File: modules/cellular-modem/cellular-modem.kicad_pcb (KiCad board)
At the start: 2 copper layers, 4 parts, among them J1 Bus_PCI_Express_Mini, U1 TXV0108RGYR, U2 TXV0108RGYR, U3 TXV0108RGYR

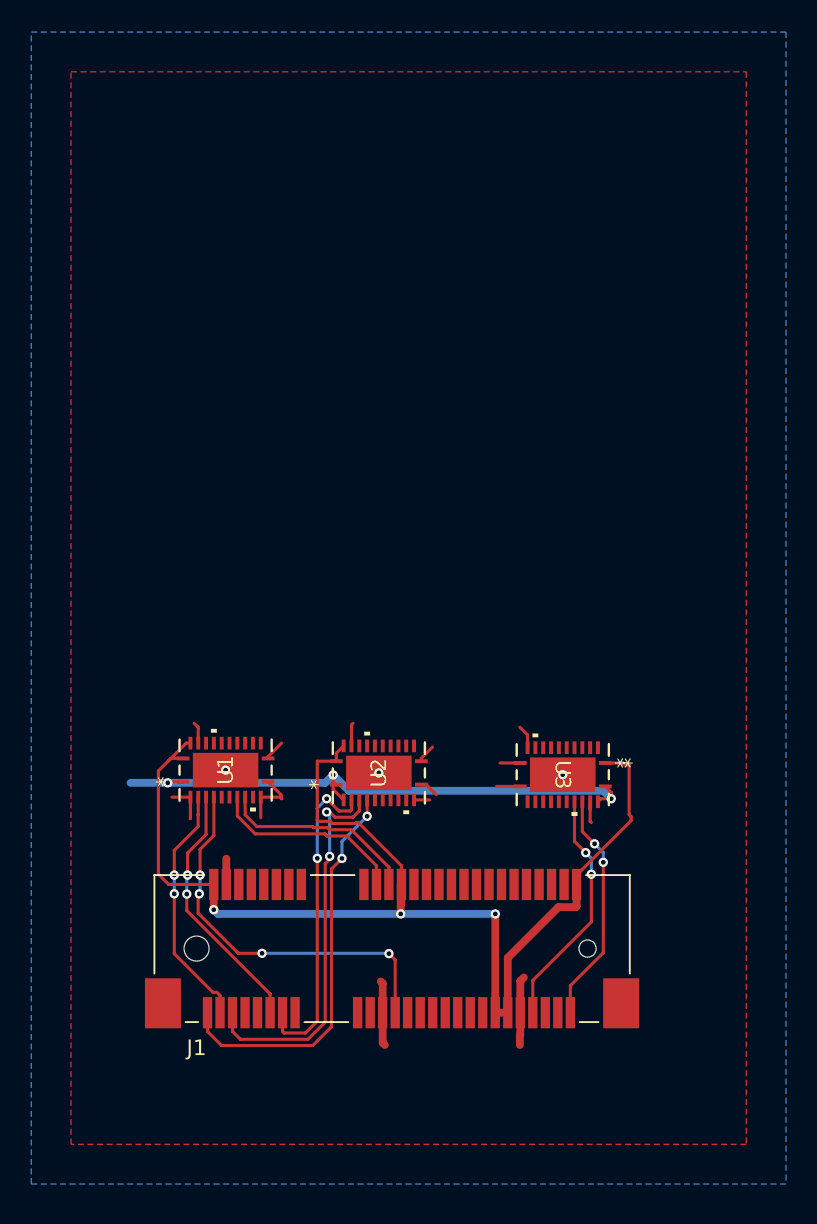
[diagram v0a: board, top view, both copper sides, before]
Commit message: layout USB lines to alegedly have correct impedance
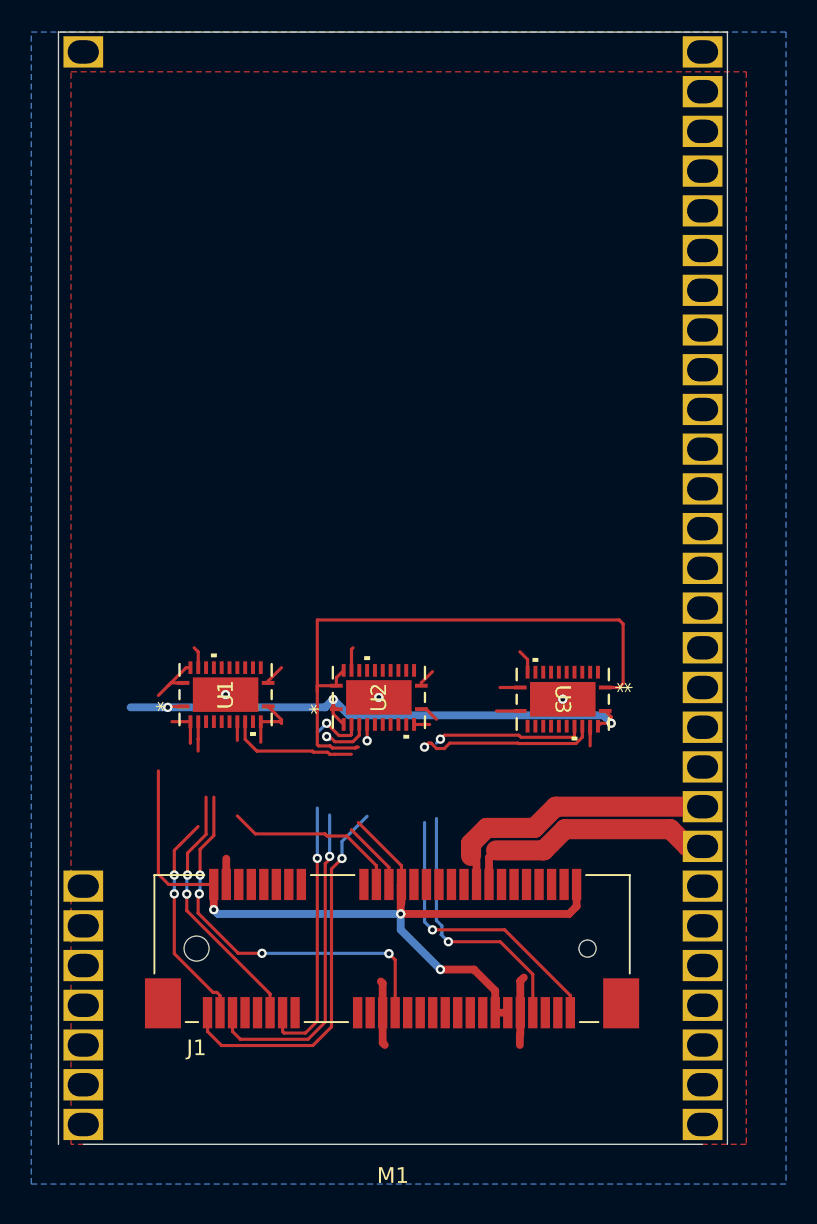
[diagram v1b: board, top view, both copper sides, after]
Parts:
- added M1: ~, MegaCastle:MegaCastle2x28-Module-I36.0x66.3-M800007FFFFFFFF-NIBBLE, F.Cu at (89.2, 71.1)
- moved U1 4.83 mm to (78.5, 77.9)
- moved U3 4.83 mm to (100.0, 78.2)
- moved U2 4.83 mm to (88.3, 78.1)
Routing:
- net 3V3: track 79.5 -> 98.0 mm
- net USB_D-: track 0.00 -> 18.1 mm
- net USB_D+: track 0.00 -> 16.6 mm
- net /PCM_SYNC_1V8_IO: track 14.9 -> 30.1 mm
- net /PCM_CLK_1V8_IO: track 15.5 -> 26.7 mm
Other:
- board outline added: 42.8 x 71.1 mm

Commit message: add 3.3V and 1.8V DC:DC to cellular modem module
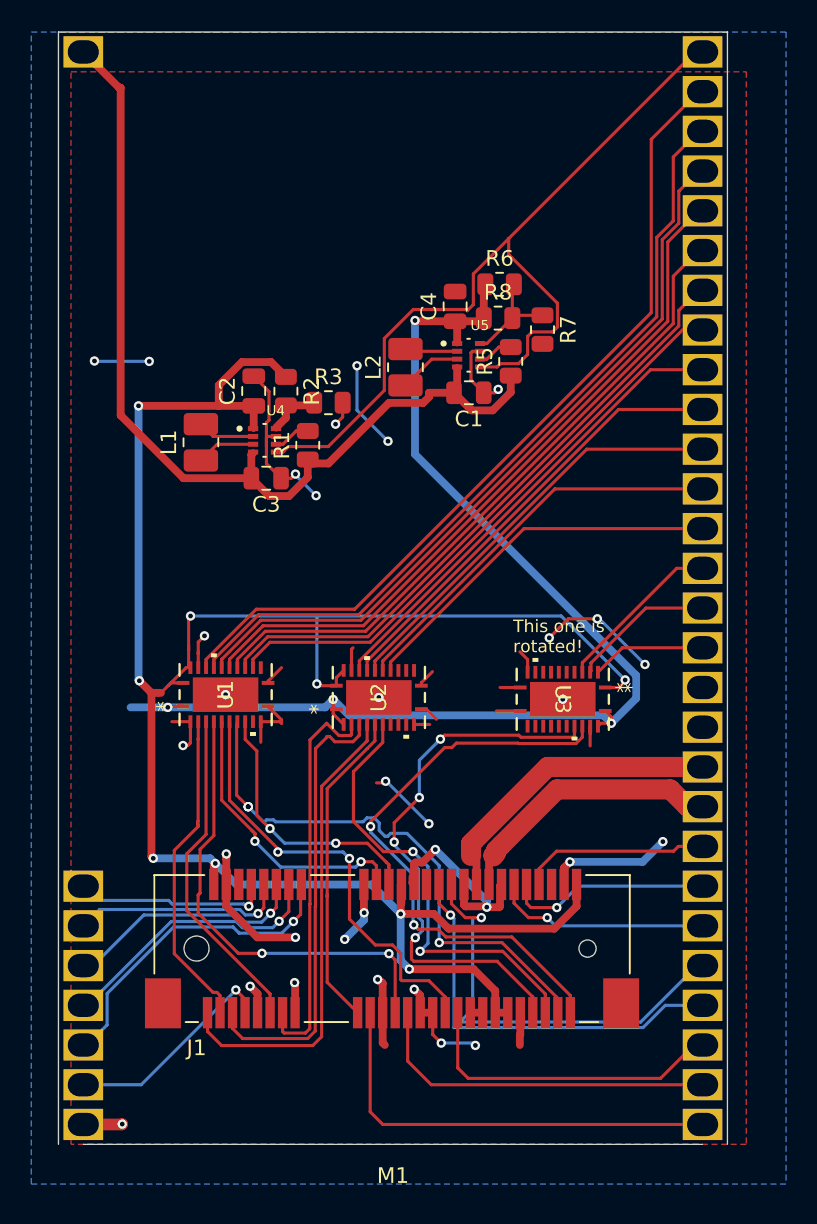
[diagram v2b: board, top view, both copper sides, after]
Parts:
- added C1: 47uF, Capacitor_SMD:C_0805_2012Metric, F.Cu at (94.0, 58.6)
- added C2: 15uF, Capacitor_SMD:C_0805_2012Metric, F.Cu at (80.3, 58.5)
- added C3: 47uF, Capacitor_SMD:C_0805_2012Metric, F.Cu at (81.1, 64.1)
- added C4: 15uF, Capacitor_SMD:C_0805_2012Metric, F.Cu at (93.1, 53.1)
- added L1: 1uH, Inductor_SMD:L_1008_2520Metric_Pad1.43x2.20mm_HandSolder, F.Cu at (76.9, 61.8)
- added L2: 1uH, Inductor_SMD:L_1008_2520Metric_Pad1.43x2.20mm_HandSolder, F.Cu at (90.0, 57.0)
- added R1: 510K, Resistor_SMD:R_0805_2012Metric, F.Cu at (83.7, 62.0)
- added R2: 510K, Resistor_SMD:R_0805_2012Metric, F.Cu at (82.3, 58.5)
- added R3: 90.9K, Resistor_SMD:R_0805_2012Metric, F.Cu at (85.0, 59.3)
- added R5: 510K, Resistor_SMD:R_0805_2012Metric, F.Cu at (96.7, 56.6)
- added R6: 510K, Resistor_SMD:R_0805_2012Metric, F.Cu at (96.0, 51.7)
- added R7: 90.9K, Resistor_SMD:R_0805_2012Metric, F.Cu at (98.7, 54.6)
- added R8: 432K, Resistor_SMD:R_0805_2012Metric, F.Cu at (95.9, 53.8)
- added U4: TPS631000DRLR, cellular-modem:SOT50P160X60-8N, F.Cu at (81.0, 61.7)
- added U5: TPS631000DRLR, cellular-modem:SOT50P160X60-8N, F.Cu at (94.0, 56.2)
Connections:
- J1 pad 25: unconnected-(J1-PERp0-Pad25) -> PERp0
- M1 pad 22: unconnected-(M1-Pad22) -> USIM_VDD
- M1 pad 23: unconnected-(M1-Pad23) -> USIM_DATA
- M1 pad 24: unconnected-(M1-Pad24) -> USIM_CLK
- M1 pad 25: unconnected-(M1-Pad25) -> /USIM_RESET
- M1 pad 26: unconnected-(M1-Pad26) -> USIM_VPP
- M1 pad 27: unconnected-(M1-Pad27) -> /CLKREQ
- M1 pad 29: unconnected-(M1-Pad29) -> EN
- M1 pad 30: unconnected-(M1-Pad30) -> COEX_UART_RX_3V3
- M1 pad 31: unconnected-(M1-Pad31) -> UART_RX_3V3
- M1 pad 32: unconnected-(M1-Pad32) -> UART_CTS_3V3
- M1 pad 33: unconnected-(M1-Pad33) -> /W_DISABLE_3V3
- M1 pad 34: unconnected-(M1-Pad34) -> /DTR_SLEEP_MODE_3V3
- M1 pad 35: unconnected-(M1-Pad35) -> PCM_DIN_3V3
- M1 pad 36: unconnected-(M1-Pad36) -> /RESET_3V3
- M1 pad 37: unconnected-(M1-Pad37) -> UART_TX_3V3
- M1 pad 38: unconnected-(M1-Pad38) -> COEX_UART_TX_3V3
- M1 pad 39: unconnected-(M1-Pad39) -> /WAKE_3V3
- M1 pad 40: unconnected-(M1-Pad40) -> RI_HOST_WAKE_3V3
- M1 pad 41: unconnected-(M1-Pad41) -> PCM_DOUT_3V3
- M1 pad 42: unconnected-(M1-Pad42) -> PCM_CLK_3V3
- M1 pad 43: unconnected-(M1-Pad43) -> PCM_SYNC_3V#
- M1 pad 44: unconnected-(M1-Pad44) -> PCM_CLK_DIR
- M1 pad 47: unconnected-(M1-Pad47) -> USB_D-
- M1 pad 48: USB_D- -> USB_D+
- M1 pad 49: USB_D+ -> RESERVED_PIN46
- M1 pad 50: unconnected-(M1-Pad50) -> USIM_SIM_PRESENT_IN
- M1 pad 51: unconnected-(M1-Pad51) -> /LED_WWAN_OC_OUT
- M1 pad 52: unconnected-(M1-Pad52) -> I2C_DATA_1V8
- M1 pad 53: unconnected-(M1-Pad53) -> I2C_SCL_1V8
- M1 pad 54: unconnected-(M1-Pad54) -> PETp0
- M1 pad 55: unconnected-(M1-Pad55) -> PERp0
- M1 pad 56: unconnected-(M1-Pad56) -> RESERVED_PIN19
- U1 pad 16: /W_DISABLE_3V3 -> PCM_DIN_3V3
- U1 pad 17: PCM_DIN_3V3 -> /DTR_SLEEP_MODE_3V3
- U1 pad 18: /DTR_SLEEP_MODE_3V3 -> /W_DISABLE_3V3
- U1 pad 6: //DTR_SLEEP_MODE_1V8_IN -> //W_DISABLE_1V8_IN
- U1 pad 7: /PCM_DIN_1V8_IN -> //DTR_SLEEP_MODE_1V8_IN
- U1 pad 8: //W_DISABLE_1V8_IN -> /PCM_DIN_1V8_IN
- U2 pad 17: RI_HOST_WAKE_3V3 -> PCM_DOUT_3V3
- U2 pad 18: PCM_DOUT_3V3 -> RI_HOST_WAKE_3V3
- U2 pad 6: /PCM_DOUT_1V8_OUT -> /RI_HOST_WAKE_1V8_OUT
- U2 pad 7: /RI_HOST_WAKE_1V8_OUT -> /PCM_DOUT_1V8_OUT
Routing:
- net GND: track 30.6 -> 112.5 mm, vias 3 -> 31
- net VBAT: track 0.00 -> 60.6 mm
- net EN: track 0.00 -> 54.7 mm
- net COEX_UART_RX_3V3: track 0.00 -> 53.8 mm
- net UART_RX_3V3: track 0.00 -> 51.1 mm
- net UART_CTS_3V3: track 0.00 -> 48.4 mm
- net /W_DISABLE_3V3: track 0.00 -> 45.6 mm
- net /DTR_SLEEP_MODE_3V3: track 0.00 -> 42.9 mm
- net 3V3: track 98.0 -> 138.6 mm, vias 3 -> 9
- net 1V8: track 36.6 -> 77.2 mm, vias 3 -> 4
- net PCM_DIN_3V3: track 0.00 -> 40.1 mm
- net /RESET_3V3: track 0.00 -> 38.0 mm
- net /PCM_DIN_1V8_IN: track 0.00 -> 35.2 mm, vias 0 -> 3
- net UART_TX_3V3: track 0.00 -> 30.3 mm
- net /PCM_DOUT_1V8_OUT: track 0.00 -> 28.9 mm, vias 0 -> 2
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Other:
- board text added: "This one is rotated!"

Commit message: relocate footprints to root dir of module
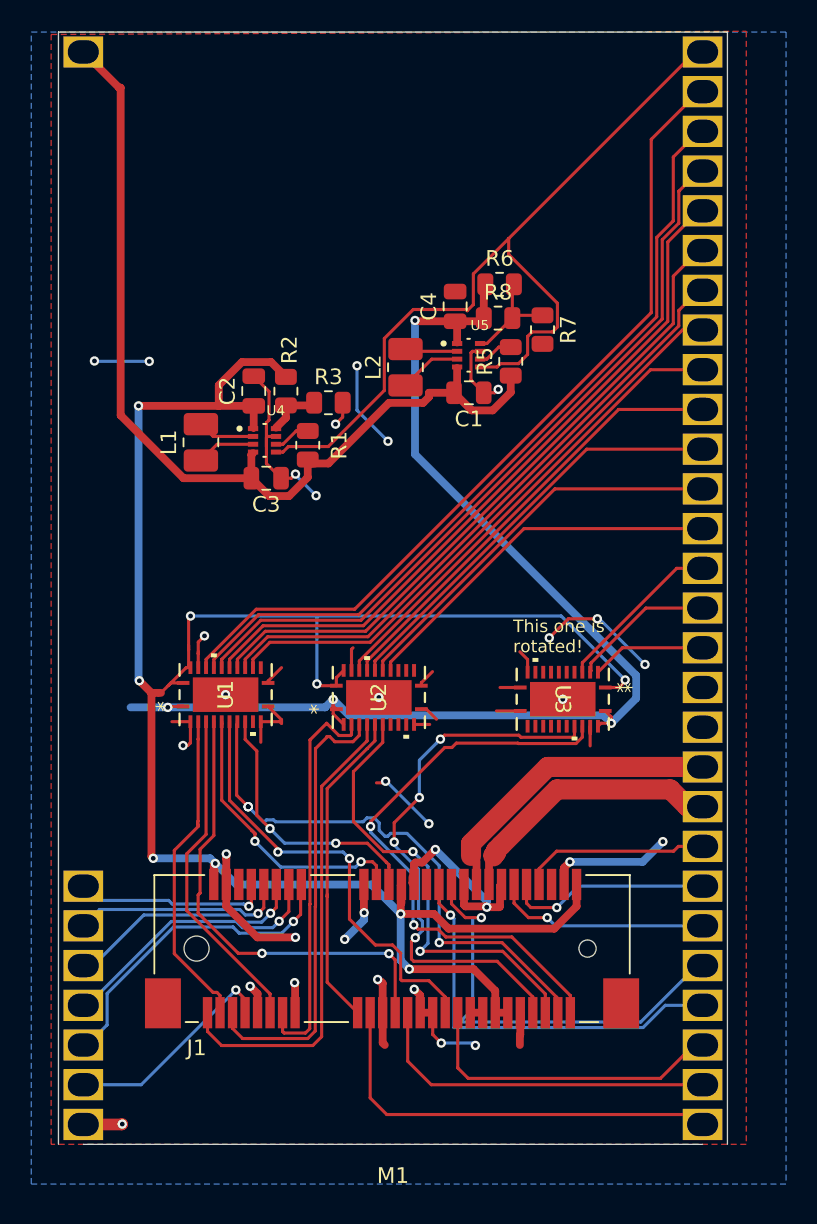
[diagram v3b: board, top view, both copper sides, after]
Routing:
- net RESERVED_PIN19: track 27.9 -> 27.4 mm
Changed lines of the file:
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@@
 		)
 		(property "Value" "TPS631000DRLR"
-			(at 4.781 1.8436 0)
-			(layer "F.Fab")
+			(at -2.2152 1.83316 90)
+			(layer "B.SilkS")
 			(effects
 				(font
@@
 					(thickness 0.15)
 				)
+				(justify mirror)
 			)
 		)
@@
 		)
 		(property "Value" "1uH"
-			(at 0 2.05 90)
-			(layer "F.Fab")
+			(at 0 0 90)
+			(layer "B.SilkS")
 			(effects
 				(font
@@
 					(thickness 0.15)
 				)
+				(justify mirror)
 			)
 		)
@@
 		)
 		(property "Value" "90.9K"
-			(at 0 1.65 90)
-			(layer "F.Fab")
+			(at 0 0 90)
+			(layer "B.SilkS")
 			(effects
 				(font
@@
 					(thickness 0.15)
 				)
+				(justify mirror)
 			)
 		)
@@
 		)
 		(property "Value" "47uF"
-			(at 0 1.68 360)
-			(layer "F.Fab")
+			(at 0.0406 -0.4318 0)
+			(layer "B.SilkS")
 			(effects
 				(font
@@
 					(thickness 0.15)
 				)
+				(justify mirror)
 			)
 		)
@@
 		)
 		(property "Value" "510K"
-			(at 0 1.65 90)
-			(layer "F.Fab")
+			(at 0 0.4572 90)
+			(layer "B.SilkS")
 			(effects
 				(font
@@
 					(thickness 0.15)
 				)
+				(justify mirror)
 			)
 		)
@@
 		)
 		(property "Value" "432K"
-			(at 0 1.65 0)
-			(layer "F.Fab")
+			(at 0 0 0)
+			(layer "B.SilkS")
 			(effects
 				(font
@@
 					(thickness 0.15)
 				)
+				(justify mirror)
 			)
 		)
@@
 		)
 		(property "Value" "1uH"
-			(at 0 2.05 90)
-			(layer "F.Fab")
+			(at 0 0 90)
+			(layer "B.SilkS")
 			(effects
 				(font
@@
 					(thickness 0.15)
 				)
+				(justify mirror)
 			)
 		)
@@
 		)
 		(property "Value" "510K"
-			(at 0 1.65 0)
-			(layer "F.Fab")
+			(at 0 0 0)
+			(layer "B.SilkS")
 			(effects
 				(font
@@
 					(thickness 0.15)
 				)
+				(justify mirror)
 			)
 		)
@@
 		)
 		(property "Value" "90.9K"
-			(at 0 1.65 360)
-			(layer "F.Fab")
+			(at 0.6858 -0.20464 0)
+			(layer "B.SilkS")
 			(effects
 				(font
@@
 					(thickness 0.15)
 				)
+				(justify mirror)
 			)
 		)
@@
 		(tags "resistor")
 		(property "Reference" "R1"
-			(at 0 -1.65 90)
+			(at 0 2.0066 90)
 			(layer "F.SilkS")
 			(effects
@@
 		)
 		(property "Value" "510K"
-			(at 0 1.65 90)
-			(layer "F.Fab")
+			(at 0 0.1016 90)
+			(layer "B.SilkS")
 			(effects
 				(font
@@
 					(thickness 0.15)
 				)
+				(justify mirror)
 			)
 		)
@@
 		(tags "resistor")
 		(property "Reference" "R2"
-			(at 0 -1.65 90)
+			(at -2.64114 -0.2286 90)
 			(layer "F.SilkS")
 			(effects
@@
 		)
 		(property "Value" "510K"
-			(at 0 1.65 90)
-			(layer "F.Fab")
+			(at -0.10114 -0.2286 90)
+			(layer "B.SilkS")
 			(effects
 				(font
@@
 					(thickness 0.15)
 				)
+				(justify mirror)
 			)
 		)
@@
 		)
 		(property "Value" "TPS631000DRLR"
-			(at 4.781 1.8436 0)
-			(layer "F.Fab")
+			(at -2.5638 2.1964 90)
+			(layer "B.SilkS")
 			(effects
 				(font
@@
 					(thickness 0.15)
 				)
+				(justify mirror)
 			)
 		)
@@
 		)
 		(property "Value" "15uF"
-			(at 0 1.68 90)
-			(layer "F.Fab")
+			(at 0 0 90)
+			(layer "B.SilkS")
 			(effects
 				(font
@@
 					(thickness 0.15)
 				)
+				(justify mirror)
 			)
 		)
@@
 		)
 		(property "Value" "15uF"
-			(at 0 1.68 90)
-			(layer "F.Fab")
+			(at 0 0 90)
+			(layer "B.SilkS")
 			(effects
 				(font
@@
 					(thickness 0.15)
 				)
+				(justify mirror)
 			)
 		)
@@
 		)
 		(property "Value" "47uF"
-			(at 0 1.68 360)
-			(layer "F.Fab")
+			(at -0.2184 -0.68436 0)
+			(layer "B.SilkS")
 			(effects
 				(font
@@
 					(thickness 0.15)
 				)
+				(justify mirror)
 			)
 		)
@@
 	)
 	(segment
-		(start 88.519 105.41)
+		(start 87.709 98.263)
+		(end 87.709 103.711)
+		(width 0.2)
+		(layer "F.Cu")
+		(net 31)
+	)
+	(segment
+		(start 108.331 104.775)
 		(end 108.966 105.41)
 		(width 0.2)
@@
 	)
 	(segment
-		(start 87.709 98.263)
-		(end 87.709 104.6)
+		(start 88.773 104.775)
+		(end 108.331 104.775)
 		(width 0.2)
 		(layer "F.Cu")
@@
 	)
 	(segment
-		(start 87.709 104.6)
-		(end 88.519 105.41)
+		(start 87.709 103.711)
+		(end 88.773 104.775)
 		(width 0.2)
 		(layer "F.Cu")
@@
 		(polygon
 			(pts
-				(xy 68.58 38.1) (xy 111.76 38.1) (xy 111.76 106.68) (xy 68.58 106.68)
+				(xy 67.31 35.7124) (xy 111.76 35.5092) (xy 111.76 106.68) (xy 67.31 106.68)
 			)
 		)

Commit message: add footprints etc for miniPCIe connector
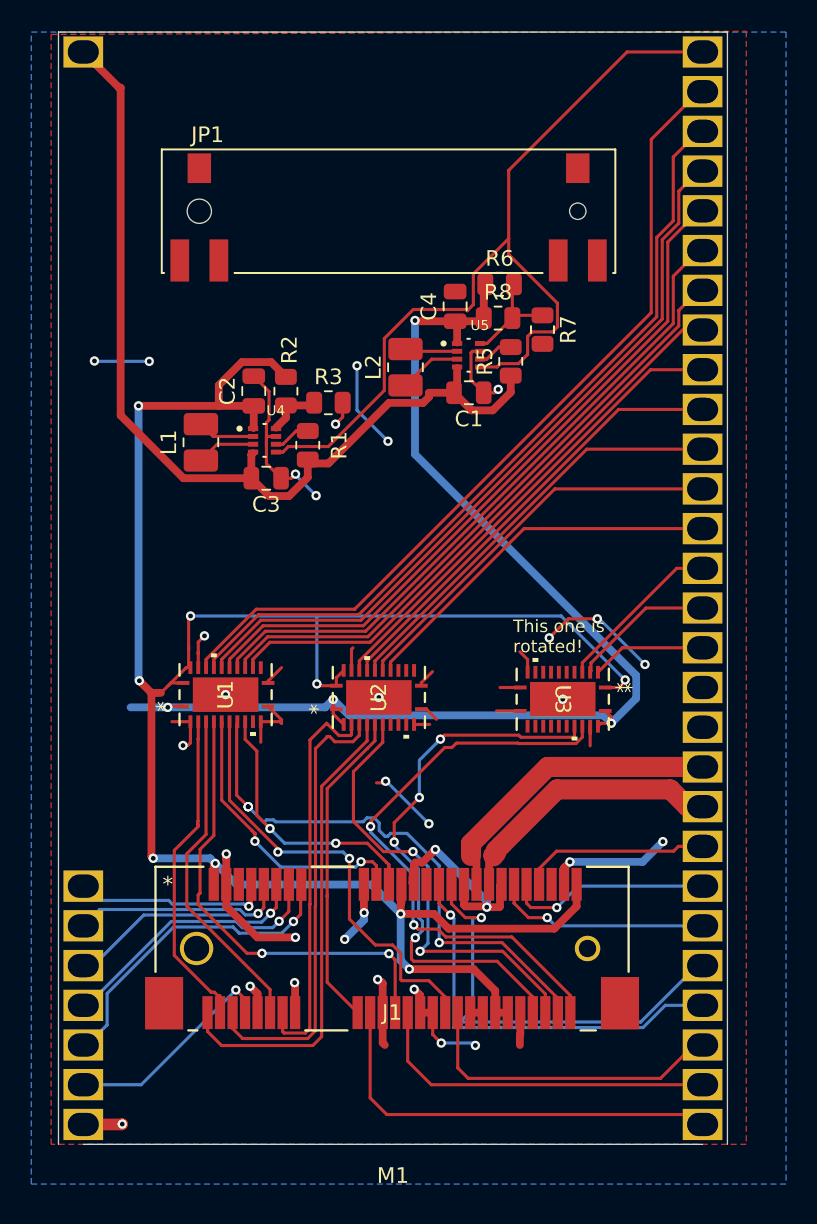
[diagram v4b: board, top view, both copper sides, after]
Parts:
- added JP1: Mini PCIe Retainer, cellular-modem:JAE_MM60-EZH059-B5-R650, F.Cu at (88.9, 47.0)
- J1: footprint Connector_PCBEdge:BUS_PCI_Express_Mini_Dual -> cellular-modem:CONN_MM60-52B1-E1-R650_JAE
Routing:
- net EN: track 54.7 -> 57.2 mm
- net /COEX_UART_RX_1V8_IN: track 20.6 -> 21.7 mm

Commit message: switch to and place MM60 symbols and footprints
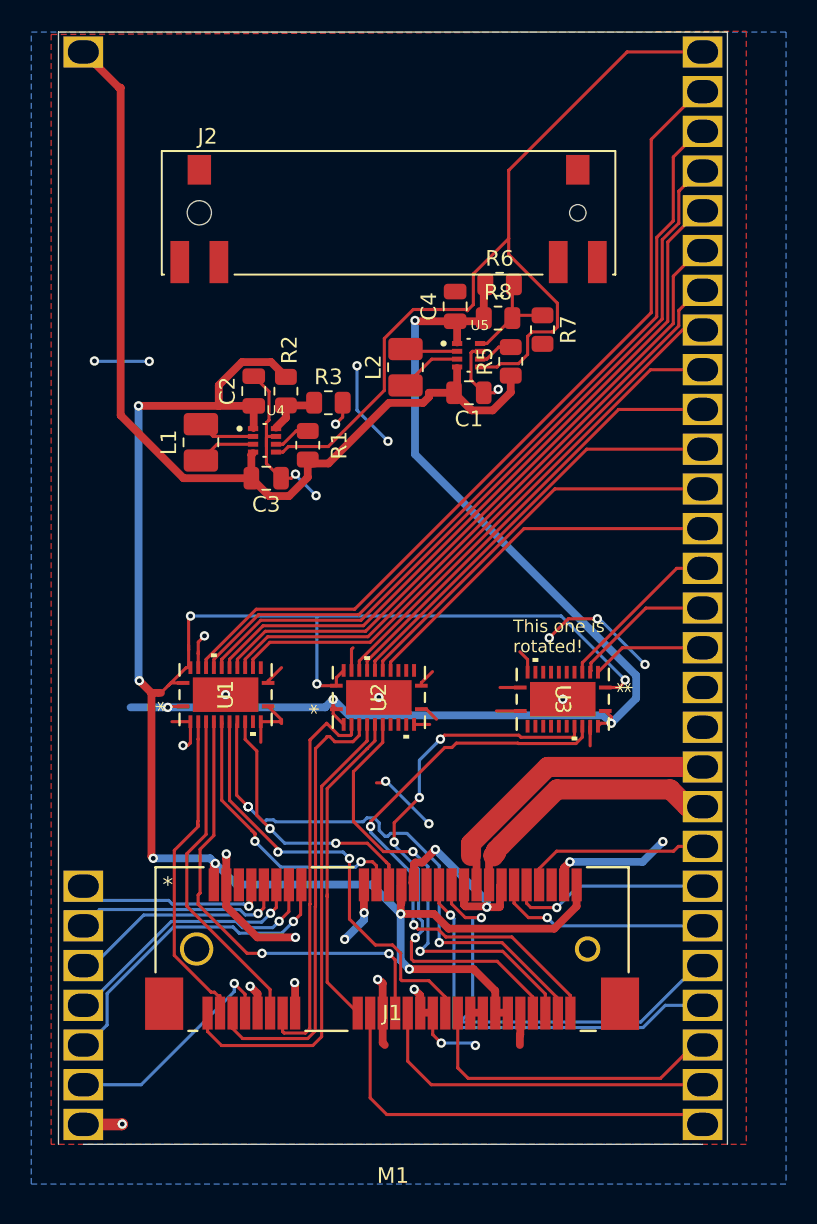
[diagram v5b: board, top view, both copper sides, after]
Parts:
- removed JP1: Mini PCIe Retainer, cellular-modem:JAE_MM60-EZH059-B5-R650
- added J2: MM60-EZH059-B5-R650, cellular-modem:JAE_MM60-EZH059-B5-R650, F.Cu at (88.9, 47.1)
- J1: value Bus_PCI_Express_Mini -> MM60-mini-PCIe
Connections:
- J1 pad 53: (no net) -> GND
- J1 pad 54: (no net) -> GND
- J1 pad 55: (no net) -> GND
- J1 pad 56: (no net) -> GND
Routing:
- net (no net): track 4.52 -> 0.00 mm, vias 2 -> 0
- net GND: track 112.5 -> 117.0 mm, vias 31 -> 33
- net /CLKREQ: track 14.0 -> 14.8 mm
